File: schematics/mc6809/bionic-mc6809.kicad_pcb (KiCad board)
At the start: 2 copper layers, 25.4 x 68.6 mm, 9 parts, among them J1 Bionic-P135, J2 Bionic-P245, U1 MC6809P, U2 11AA010-I/TT

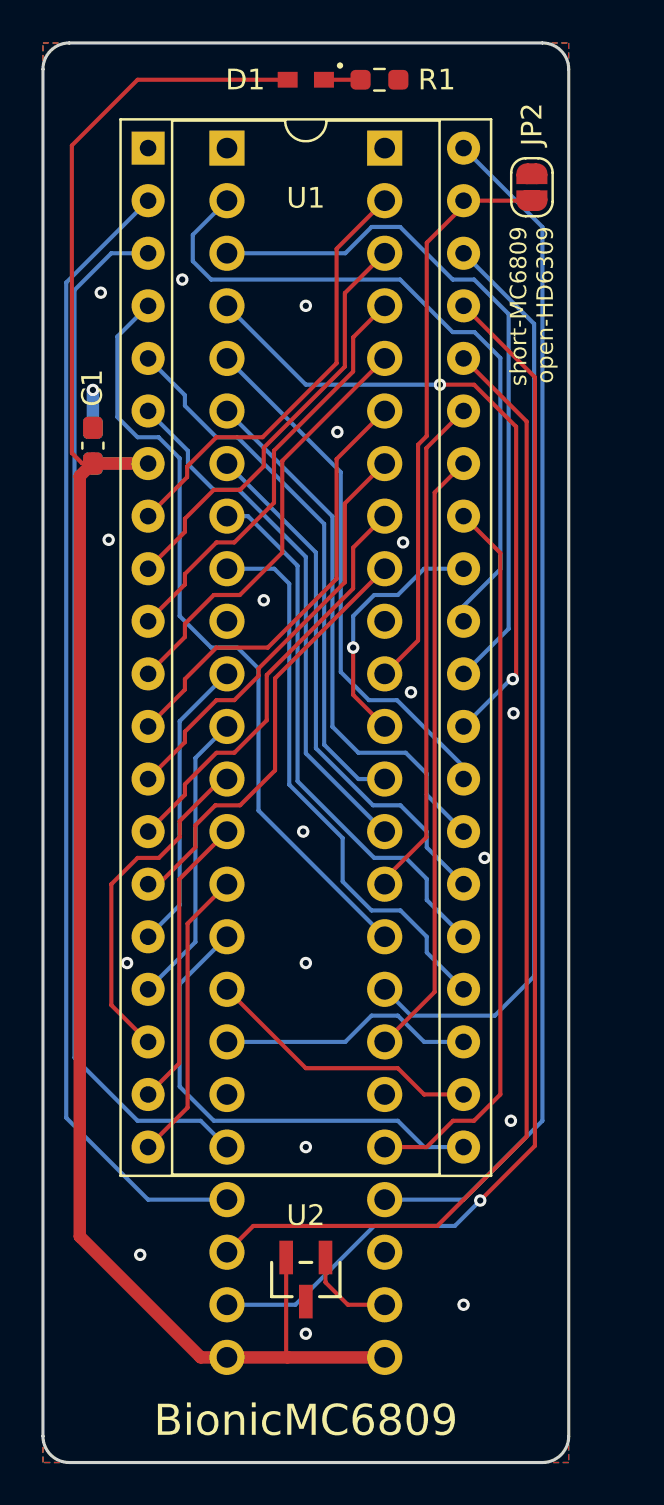
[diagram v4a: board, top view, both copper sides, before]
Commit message: [MC6809] Update schematics
Remove unused pins from bionic connector
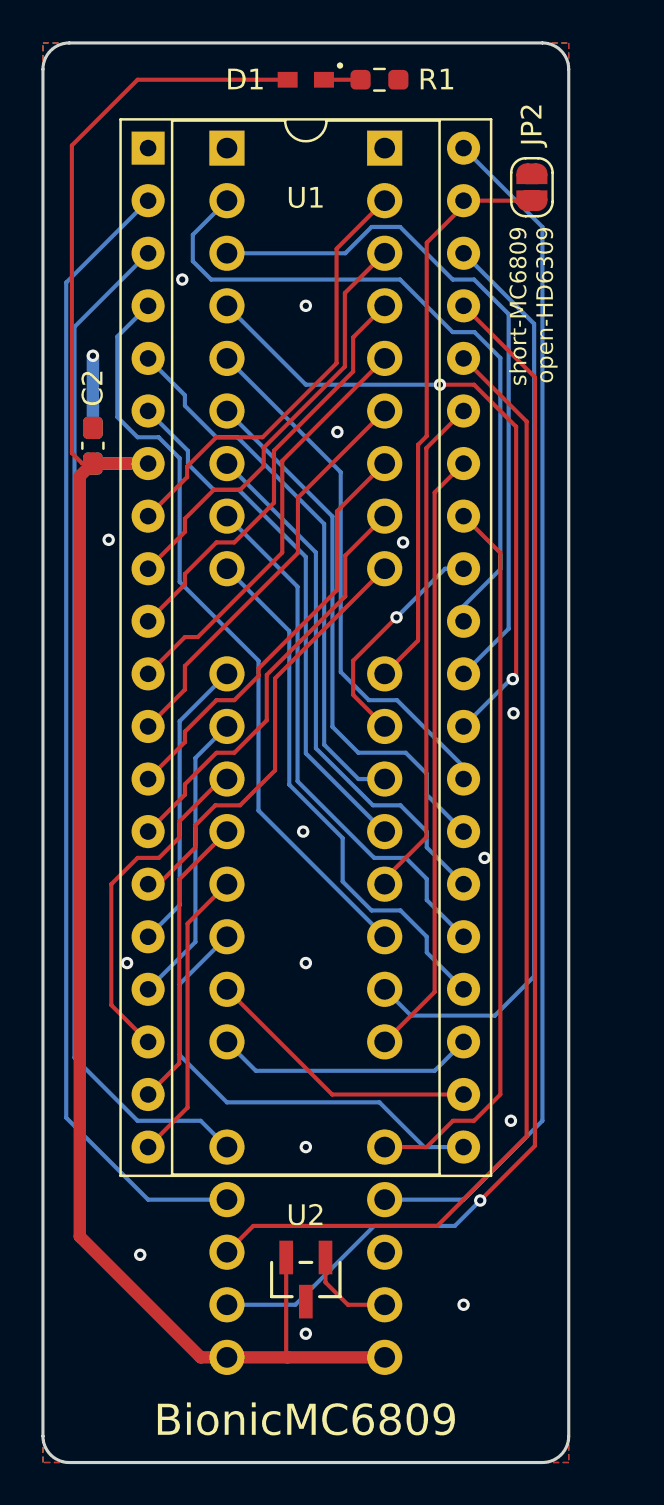
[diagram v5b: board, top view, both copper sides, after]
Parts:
- C1: moved to B.Cu
- C2: moved to F.Cu
- J1: footprint bionic:Bionic-P135_Vertical -> bionic:Bionic-P135_THT
- J2: footprint bionic:Bionic-P245_Vertical -> bionic:Bionic-P245_THT
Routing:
- net GND: track 1.80 -> 3.46 mm, vias 19 -> 16
- net /P24: track 21.4 -> 20.0 mm
- net /P17: track 27.2 -> 25.9 mm
- net /P41: track 12.5 -> 11.2 mm
- net /P50: track 50.5 -> 49.5 mm
- net /P35: track 23.1 -> 22.2 mm
- net /P45: track 37.8 -> 37.0 mm
- net /P16: track 26.5 -> 25.9 mm
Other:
- board text added: "Rev. 7"
- board text removed: "Rev. 6"
